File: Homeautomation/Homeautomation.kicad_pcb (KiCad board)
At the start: 4 copper layers, 53.3 x 25.4 mm, 67 parts, among them J1 Conn_01x02, U1 STM32F437VITx, U2 TPS22810, U3 INA214, U4 AT25SF081-SSHD-X, U5 LAN8742_INT, X1 JXD1-0007NL, X2 HA_MAIN_IF, X3 Conn_01x06_Female, X4 SG-210SED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

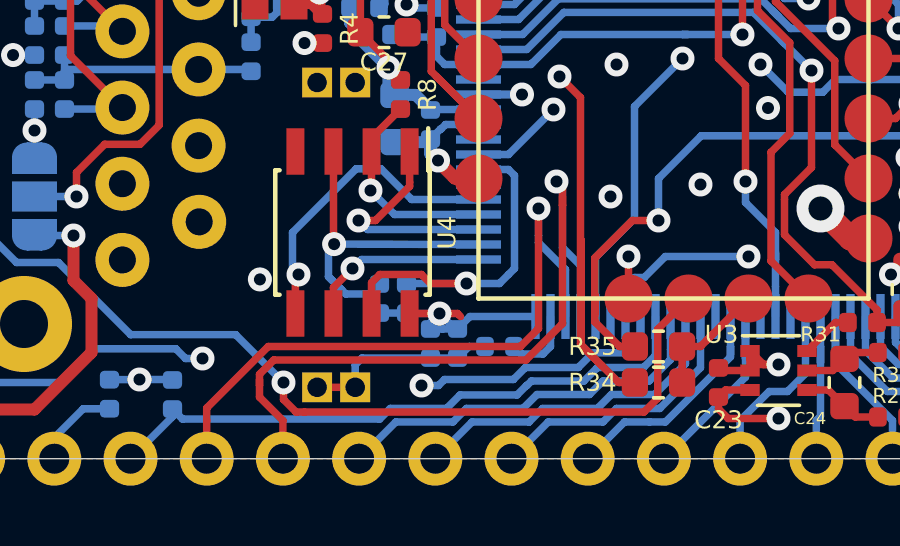
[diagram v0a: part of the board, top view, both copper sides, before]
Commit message: Update HA Files  Homeautomation: Add 3V3A to Ethernet Connector
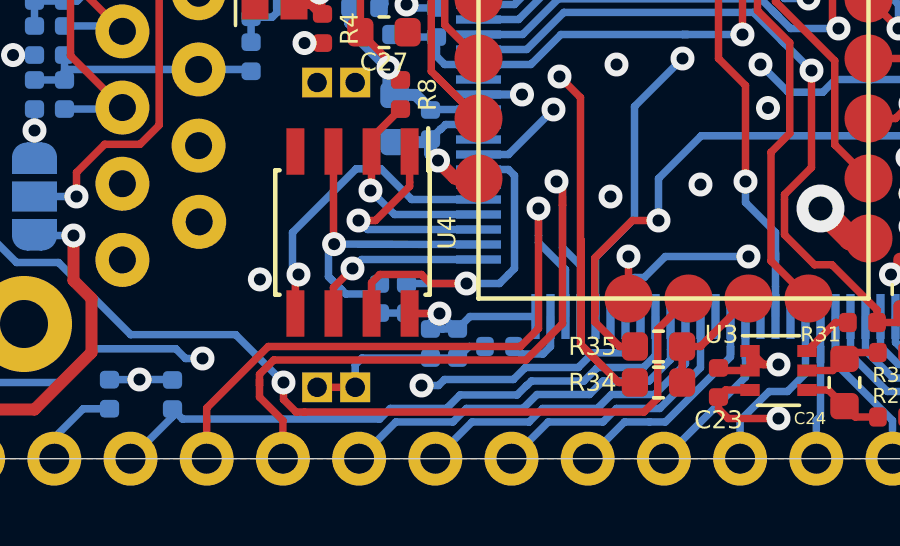
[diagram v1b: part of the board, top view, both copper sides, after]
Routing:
- net +3V3: track 238.3 -> 237.6 mm
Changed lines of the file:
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@@
     (thickness 1.6)
     (drawings 4)
-    (tracks 1281)
+    (tracks 1279)
     (zones 0)
     (modules 67)
@@
   (segment (start 176.4 129.7) (end 175.13 129.7) (width 0.8) (layer In1.Cu) (net 1))
   (segment (start 175.414315 138.26) (end 175.88 138.26) (width 0.8) (layer In1.Cu) (net 1))
-  (segment (start 155.68 147.56) (end 155.78 147.66) (width 0.25) (layer F.Cu) (net 1))
   (segment (start 154.085 147.56) (end 155.08 147.56) (width 0.25) (layer F.Cu) (net 1))
   (via (at 151.08 135.66) (size 0.8) (drill 0.4) (layers F.Cu B.Cu) (net 1))
@@
   (segment (start 153.08 147.545) (end 153.98 147.545) (width 0.25) (layer B.Cu) (net 1))
   (segment (start 146.68 149.76) (end 145.08 149.76) (width 0.4) (layer In1.Cu) (net 1))
-  (segment (start 155.08 147.56) (end 155.68 147.56) (width 0.25) (layer F.Cu) (net 1))
   (via (at 155.08 147.56) (size 0.8) (drill 0.4) (layers F.Cu B.Cu) (net 1))
   (segment (start 156.095 147.66) (end 155.68 148.075) (width 0.25) (layer B.Cu) (net 1))
@@
   (segment (start 160.28 130.55077) (end 158.864251 129.135021) (width 0.25) (layer B.Cu) (net 8))
   (segment (start 160.28 131.86) (end 160.28 130.55077) (width 0.25) (layer B.Cu) (net 8))
-  (segment (start 141.58 139.775) (end 142.58 139.775) (width 0.25) (layer B.Cu) (net 114))
-  (segment (start 142.58 139.46) (end 142.615 139.425) (width 0.25) (layer B.Cu) (net 114))
-  (segment (start 142.58 139.46) (end 142.58 139.775) (width 0.25) (layer B.Cu) (net 114))
-  (segment (start 142.615 139.425) (end 147.05 139.425) (width 0.25) (layer B.Cu) (net 114))
-  (segment (start 142.58 138.945) (end 142.58 139.46) (width 0.25) (layer B.Cu) (net 114))
   (segment (start 141.58 137.975) (end 141.58 137.145) (width 0.25) (layer B.Cu) (net 9))
   (segment (start 141.58 137.145) (end 142.58 137.145) (width 0.25) (layer B.Cu) (net 9))
@@
   (segment (start 154.804989 139.484989) (end 154.804989 136.686987) (width 0.25) (layer F.Cu) (net 113))
   (segment (start 156.38 141.06) (end 154.804989 139.484989) (width 0.25) (layer F.Cu) (net 113))
+  (segment (start 141.58 139.775) (end 142.58 139.775) (width 0.25) (layer B.Cu) (net 114))
+  (segment (start 142.58 139.46) (end 142.615 139.425) (width 0.25) (layer B.Cu) (net 114))
+  (segment (start 142.58 139.46) (end 142.58 139.775) (width 0.25) (layer B.Cu) (net 114))
+  (segment (start 142.615 139.425) (end 147.05 139.425) (width 0.25) (layer B.Cu) (net 114))
+  (segment (start 142.58 138.945) (end 142.58 139.46) (width 0.25) (layer B.Cu) (net 114))
   (segment (start 144.33 137.975) (end 144.51 138.155) (width 0.25) (layer B.Cu) (net 114))
   (segment (start 142.58 137.975) (end 144.33 137.975) (width 0.25) (layer B.Cu) (net 114))
